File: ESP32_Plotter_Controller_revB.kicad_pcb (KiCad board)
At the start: 2 copper layers, 99.1 x 55.4 mm, 48 parts, among them J1 ARM JTAG 10pin, J10 Pen Lift, J11 Vselect, J12 X Motor, J13 Y Motor, J14 Neo Pixel LEDs, J15 Pen Direction, J16 Aux Port (I2C), J17 USB_B_Micro, J18 E-Stop, J2 Power, J3 5V Aux, J4 Vin Aux, J5 Limit Switches, J6 Aux Port (SPI), J7 X Limit, J8 Micro_SD_Card, J9 Y Limit, SW1 RESET, SW2 BOOT, U1 ESP32-WROOM-32D, U2 TMC2130, U3 TMC2130, U4 XL1509, U5 CH340C, U6 AMS1117-3.3

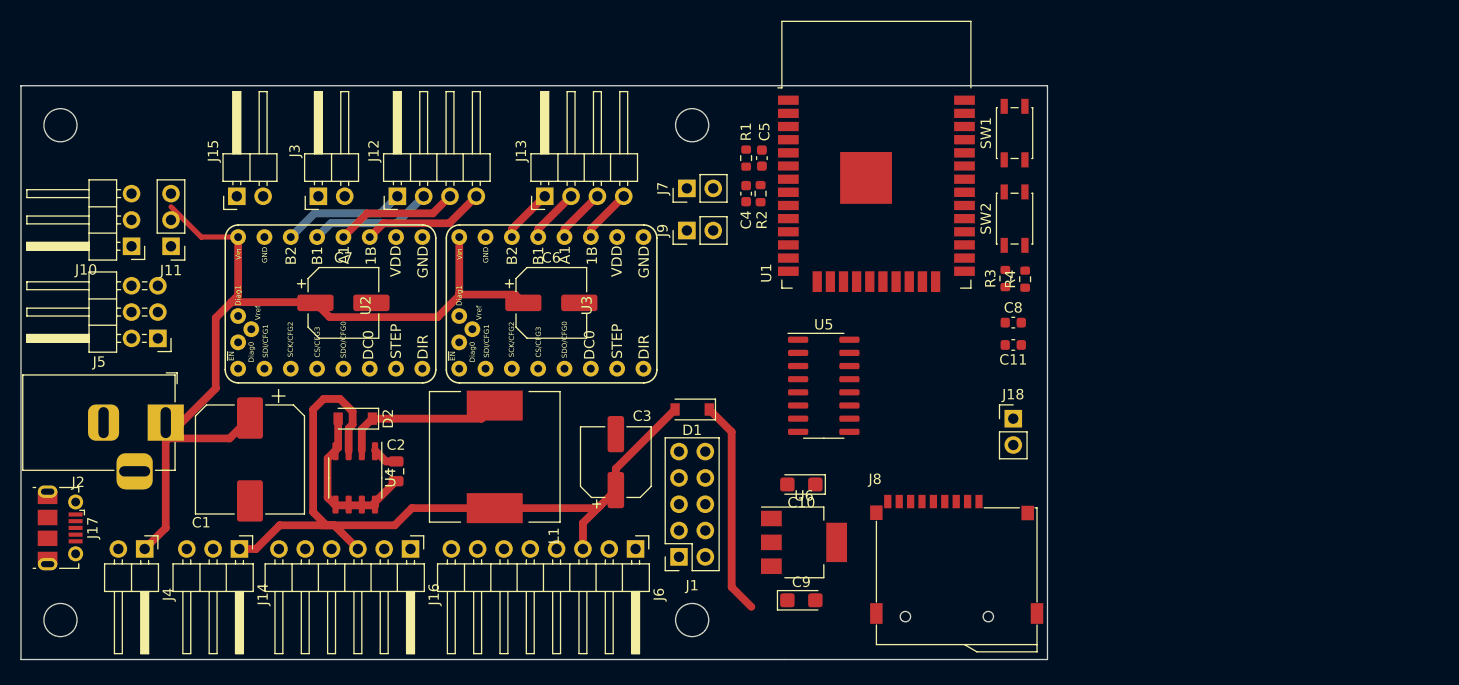
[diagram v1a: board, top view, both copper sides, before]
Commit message: First pass at placing components with JST connectors
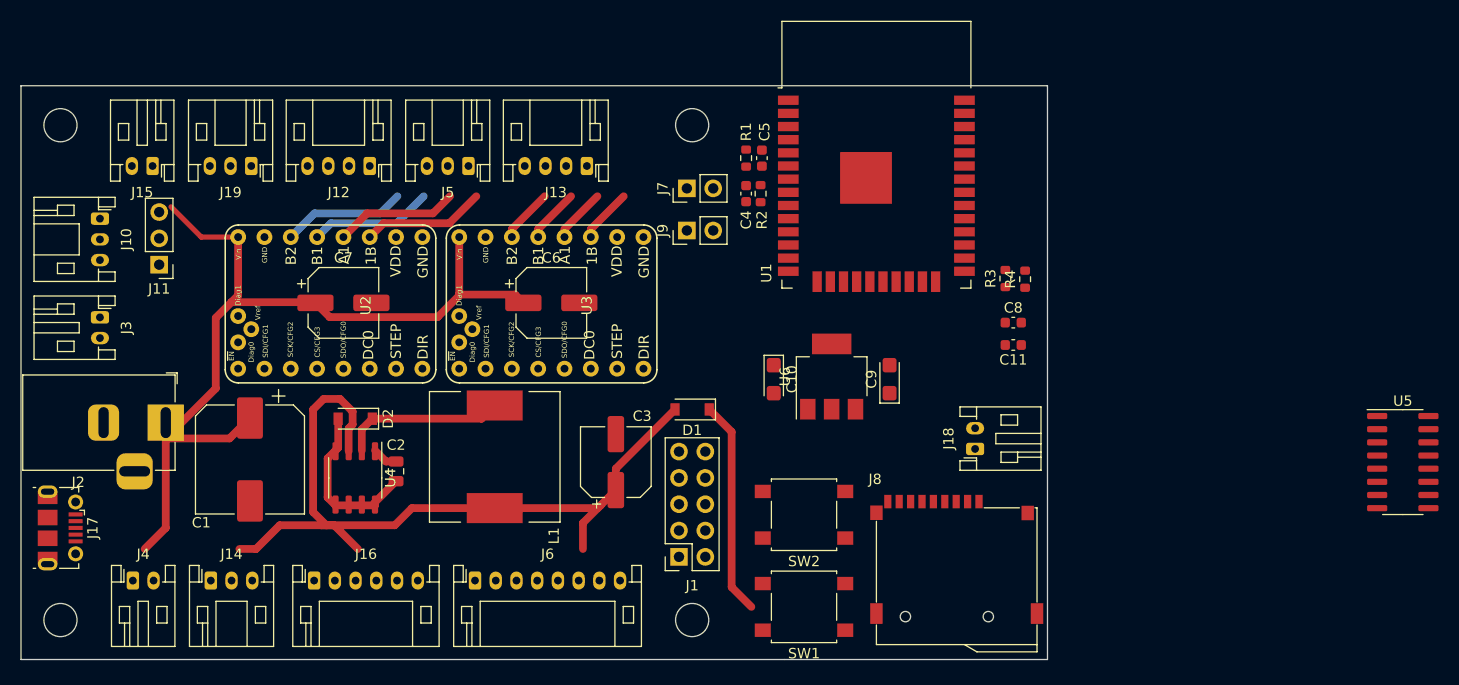
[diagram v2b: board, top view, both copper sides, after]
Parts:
- added J19: Y Limit Switch, Connector_JST:JST_PH_S3B-PH-K_1x03_P2.00mm_Horizontal, F.Cu at (47.6, 76.8)
- C10, C9: footprint Capacitor_Tantalum_SMD:CP_EIA-3216-10_Kemet-I -> Capacitor_Tantalum_SMD:CP_EIA-3216-18_Kemet-A
- J10, J14: footprint Connector_PinHeader_2.54mm:PinHeader_1x03_P2.54mm_Horizontal -> Connector_JST:JST_PH_S3B-PH-K_1x03_P2.00mm_Horizontal
- J12, J13: footprint Connector_PinHeader_2.54mm:PinHeader_1x04_P2.54mm_Horizontal -> Connector_JST:JST_PH_S4B-PH-K_1x04_P2.00mm_Horizontal
- J15, J3, J4: footprint Connector_PinHeader_2.54mm:PinHeader_1x02_P2.54mm_Horizontal -> Connector_JST:JST_PH_S2B-PH-K_1x02_P2.00mm_Horizontal
- J16: footprint Connector_PinHeader_2.54mm:PinHeader_1x06_P2.54mm_Horizontal -> Connector_JST:JST_PH_S6B-PH-K_1x06_P2.00mm_Horizontal
- J18: footprint Connector_PinHeader_2.54mm:PinHeader_1x02_P2.54mm_Vertical -> Connector_JST:JST_PH_S2B-PH-K_1x02_P2.00mm_Horizontal
- J5: value Limit Switches -> X Limit Switch; footprint Connector_PinHeader_2.54mm:PinHeader_2x03_P2.54mm_Horizontal -> Connector_JST:JST_PH_S3B-PH-K_1x03_P2.00mm_Horizontal
- J6: footprint Connector_PinHeader_2.54mm:PinHeader_1x08_P2.54mm_Horizontal -> Connector_JST:JST_PH_S8B-PH-K_1x08_P2.00mm_Horizontal
- SW1, SW2: footprint Button_Switch_SMD:SW_SPST_EVQP2 -> Button_Switch_SMD:SW_SPST_B3S-1000
- moved U5 56.4 mm to (158.8, 105.4)
- moved SW1 50.0 mm to (101.0, 119.4), turned to 180 degrees
- moved SW2 35.1 mm to (101.0, 110.5), turned to 180 degrees
- moved J5 34.3 mm to (68.6, 76.8)
- moved J3 24.1 mm to (33.0, 91.4), turned to 270 degrees
- moved C9 23.0 mm to (109.2, 97.4), turned to 90 degrees
- moved U6 16.2 mm to (103.6, 97.2), turned to 90 degrees
- moved J6 15.8 mm to (69.2, 116.8), turned to 0 degrees
- moved C10 10.5 mm to (98.0, 97.4), turned to 270 degrees
- moved J16 9.79 mm to (53.7, 116.8), turned to 0 degrees
- moved J15 8.64 mm to (38.1, 76.8), turned to 180 degrees
- moved J13 5.00 mm to (80.0, 76.8), turned to 180 degrees
- moved J18 4.70 mm to (117.5, 104.1), turned to 90 degrees
- moved J14 4.11 mm to (43.7, 116.8), turned to 0 degrees
- moved J10 4.05 mm to (33.0, 81.9), turned to 270 degrees
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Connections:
- J5 pad 1: GND -> +3V3
- J5 pad 2: GND -> Net-(J5-Pad2)
- J5 pad 3: Net-(J5-Pad3) -> GND
- R1 pad 2: Net-(J5-Pad3) -> Net-(J5-Pad2)
- R2 pad 2: Net-(J5-Pad4) -> Net-(J19-Pad2)
